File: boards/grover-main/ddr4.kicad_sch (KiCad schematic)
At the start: 3 parts

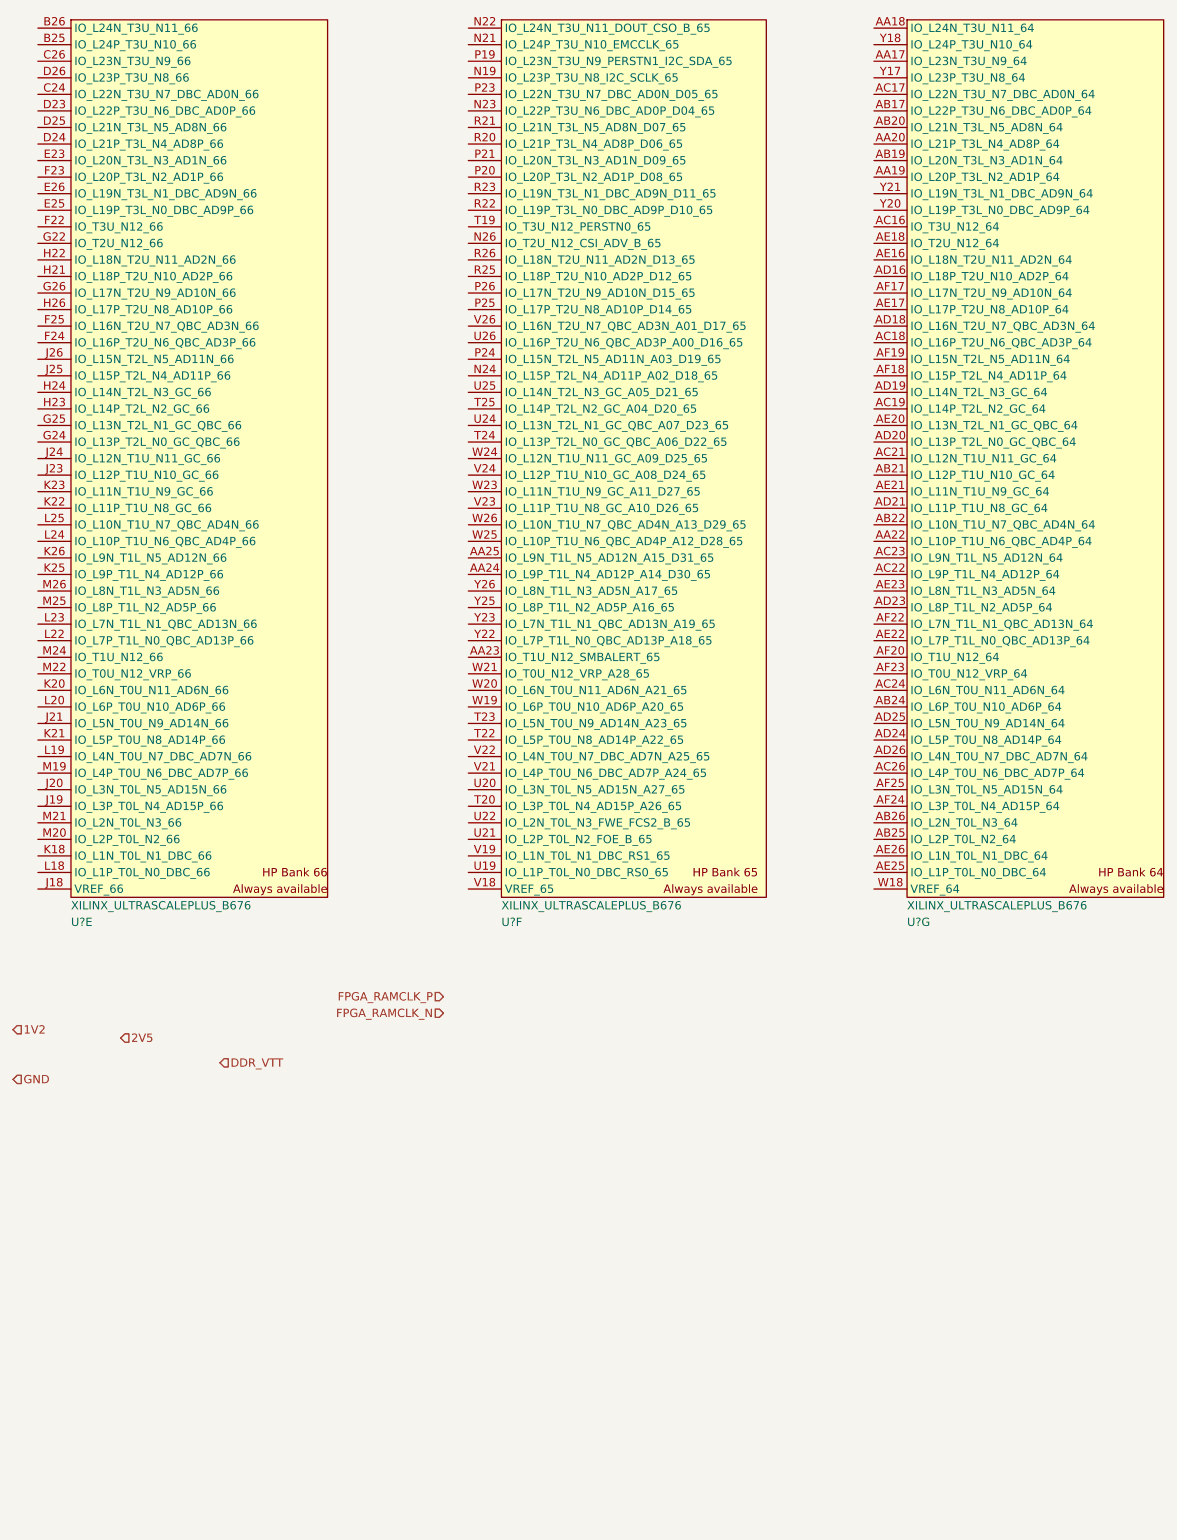
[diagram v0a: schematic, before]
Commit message: Continued initial schematic capture
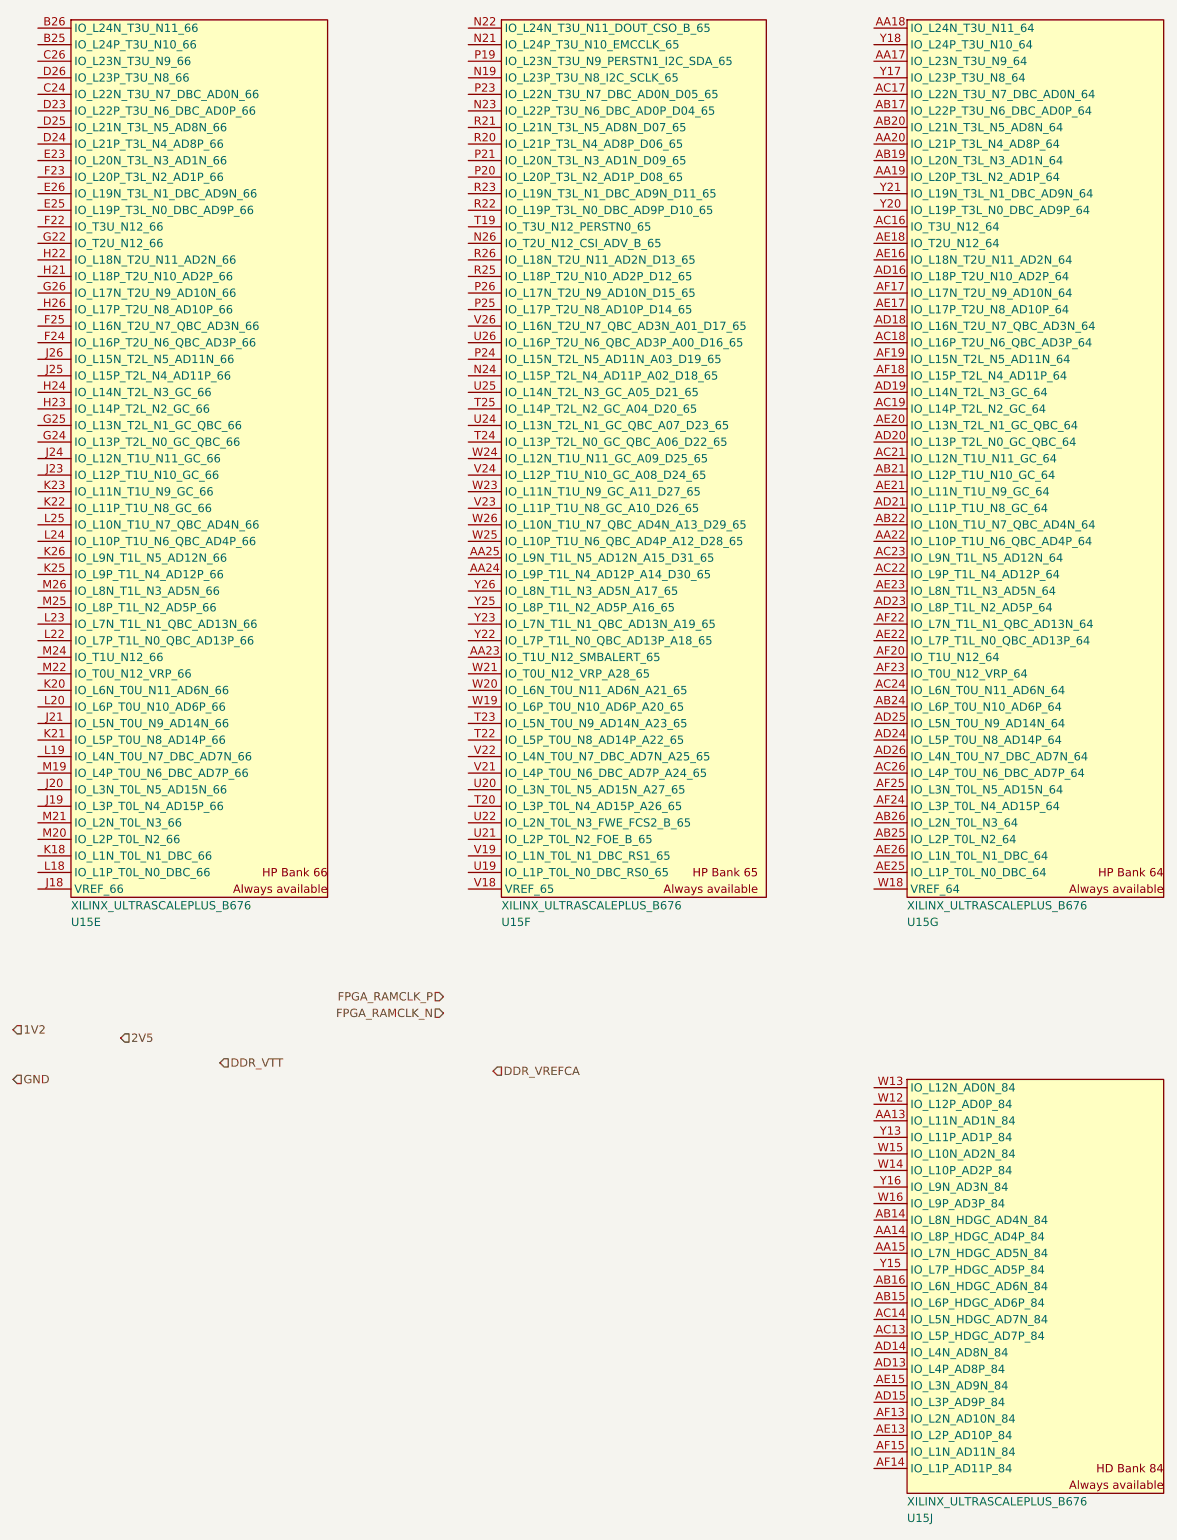
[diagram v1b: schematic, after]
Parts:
- added unit 10 of U15
- gave numbers to parts that had none: 1
